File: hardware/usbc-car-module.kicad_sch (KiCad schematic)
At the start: 0 parts

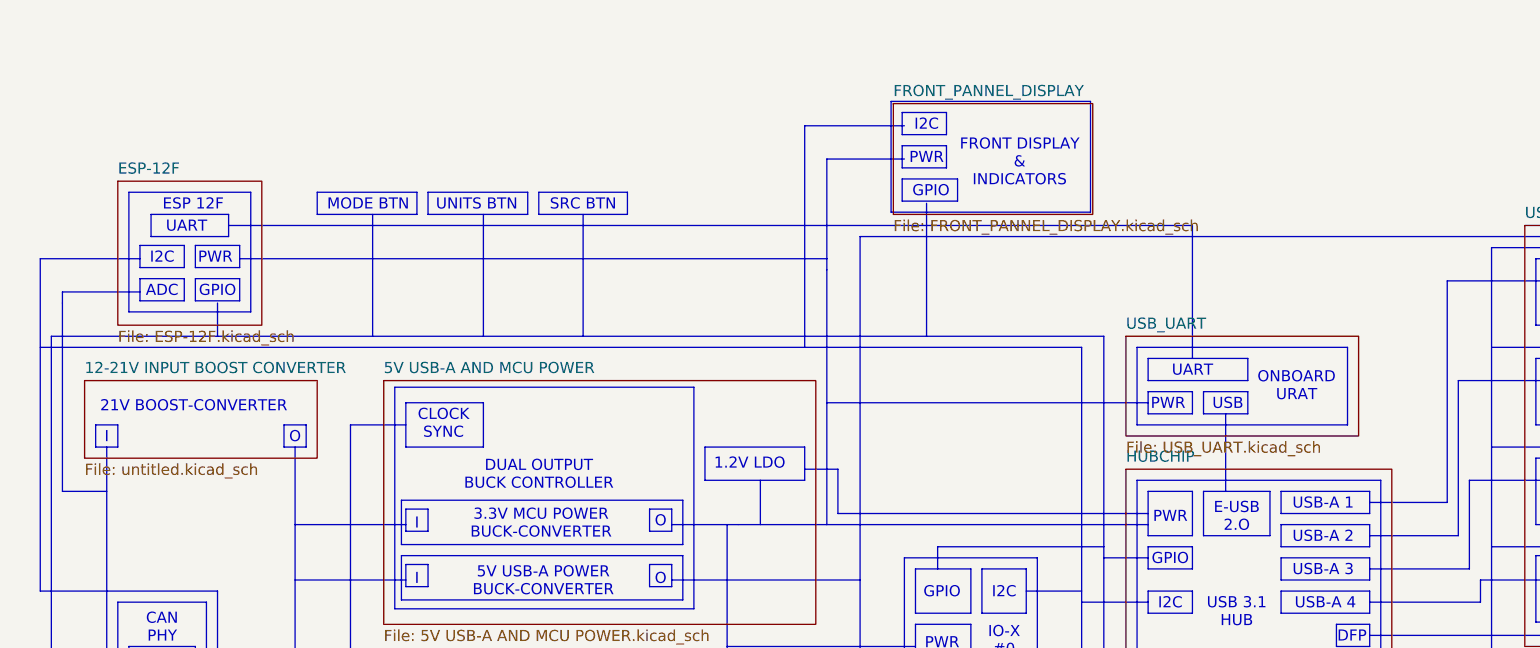
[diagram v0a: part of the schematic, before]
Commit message: migrated to the esp32-s2 and starting new board revison
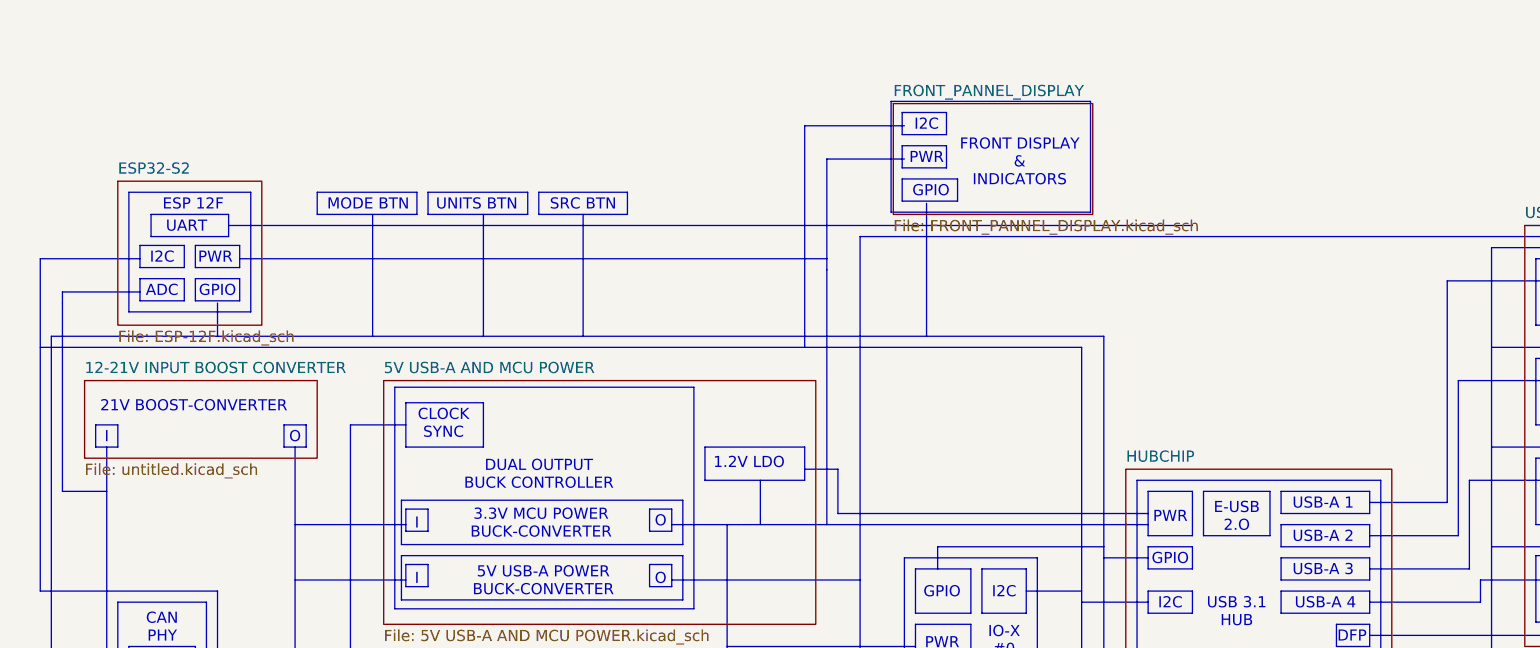
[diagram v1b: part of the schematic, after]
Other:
- sheet ESP-12F renamed ESP32-S2
- removed sheet USB_UART
- note removed: "ONBOARD URAT"
